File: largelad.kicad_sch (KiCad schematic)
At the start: 297 parts, among them SW1 RotaryEncoder_Switch, U3 YAAJ_WeAct_BlackPill_Part_Like

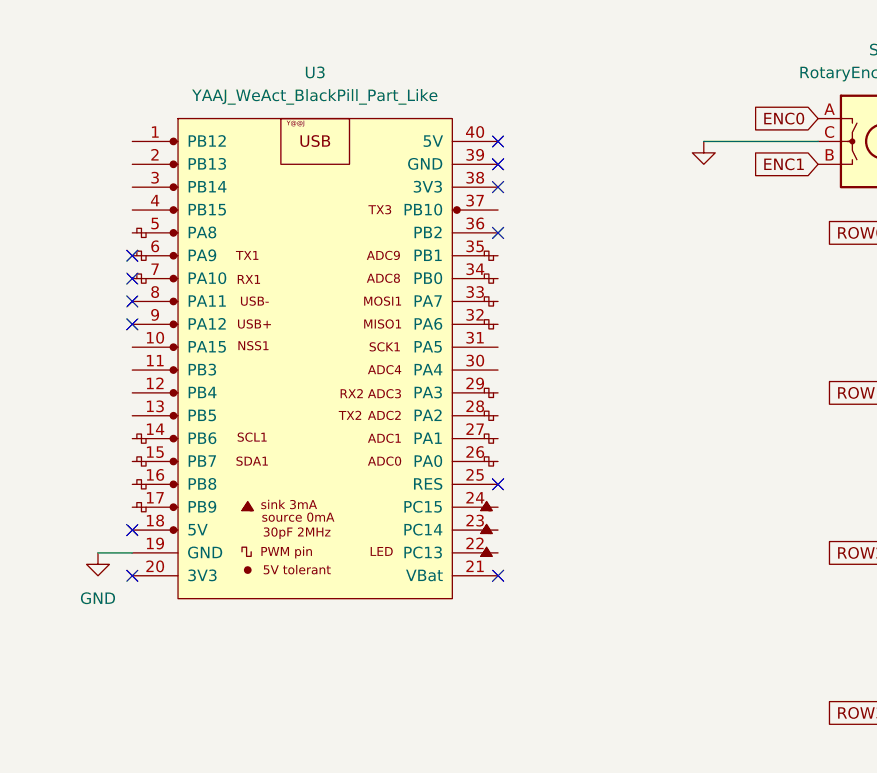
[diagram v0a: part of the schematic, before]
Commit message: connect up the columns
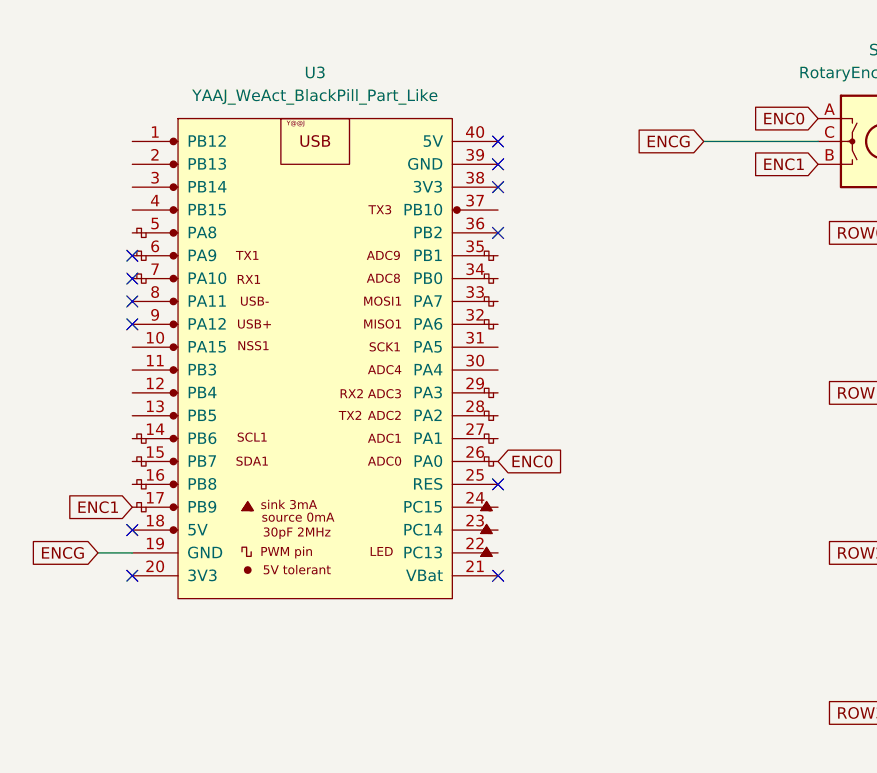
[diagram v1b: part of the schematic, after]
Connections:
- net ENC0: now also U3.26 (PA0)
- net ENC1: now also U3.17 (PB9)
- net GND renamed ENCG
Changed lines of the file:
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@@
     )
   )
+  (global_label "ENC1" (shape input) (at 96.52 74.93 180) (fields_autoplaced)
+    (effects (font (size 1.27 1.27)) (justify right))
+    (property "Intersheet References" "${INTERSHEET_REFS}" (id 0) (at 89.1479 74.8506 0)
+      (effects (font (size 1.27 1.27)) (justify right) hide)
+    )
+  )
   (global_label "COL4" (shape input) (at 240.03 30.48 90) (fields_autoplaced)
     (effects (font (size 1.27 1.27)) (justify left))
@@
     )
   )
+  (global_label "ENCG" (shape input) (at 160.02 34.29 180) (fields_autoplaced)
+    (effects (font (size 1.27 1.27)) (justify right))
+    (property "Intersheet References" "${INTERSHEET_REFS}" (id 0) (at 152.5874 34.2106 0)
+      (effects (font (size 1.27 1.27)) (justify right) hide)
+    )
+  )
   (global_label "ROW1" (shape input) (at 181.61 62.23 180) (fields_autoplaced)
     (effects (font (size 1.27 1.27)) (justify right))
@@
     )
   )
+  (global_label "ENCG" (shape input) (at 92.71 80.01 180) (fields_autoplaced)
+    (effects (font (size 1.27 1.27)) (justify right))
+    (property "Intersheet References" "${INTERSHEET_REFS}" (id 0) (at 85.2774 79.9306 0)
+      (effects (font (size 1.27 1.27)) (justify right) hide)
+    )
+  )
   (global_label "ROW7" (shape input) (at 181.61 168.91 180) (fields_autoplaced)
     (effects (font (size 1.27 1.27)) (justify right))
@@
     )
   )
+  (global_label "ENC0" (shape input) (at 137.16 69.85 0) (fields_autoplaced)
+    (effects (font (size 1.27 1.27)) (justify left))
+    (property "Intersheet References" "${INTERSHEET_REFS}" (id 0) (at 144.5321 69.9294 0)
+      (effects (font (size 1.27 1.27)) (justify left) hide)
+    )
+  )
   (global_label "ROW3" (shape input) (at 181.61 97.79 180) (fields_autoplaced)
     (effects (font (size 1.27 1.27)) (justify right))
@@
     (pin "2")
   )
-  (symbol (lib_id "power:GND") (at 92.71 80.01 0) (unit 1)
-    (in_bom yes) (on_board yes) (fields_autoplaced)
-    (property "Reference" "#PWR03" (id 0) (at 92.71 86.36 0)
-      (effects (font (size 1.27 1.27)) hide)
-    )
-    (property "Value" "GND" (id 1) (at 92.71 85.09 0))
-    (property "Footprint" "" (id 2) (at 92.71 80.01 0)
-      (effects (font (size 1.27 1.27)) hide)
-    )
-    (property "Datasheet" "" (id 3) (at 92.71 80.01 0)
-      (effects (font (size 1.27 1.27)) hide)
-    )
-    (pin "1")
-  )
   (symbol (lib_id "Device:D_Small") (at 187.96 59.69 90) (unit 1)
     (in_bom yes) (on_board yes) (fields_autoplaced)
@@
     (pin "2")
   )
-  (symbol (lib_id "power:GND") (at 160.02 34.29 0) (unit 1)
-    (in_bom yes) (on_board yes) (fields_autoplaced)
-    (property "Reference" "#PWR?" (id 0) (at 160.02 40.64 0)
-      (effects (font (size 1.27 1.27)) hide)
-    )
-    (property "Value" "" (id 1) (at 160.02 39.37 0))
-    (property "Footprint" "" (id 2) (at 160.02 34.29 0)
-      (effects (font (size 1.27 1.27)) hide)
-    )
-    (property "Datasheet" "" (id 3) (at 160.02 34.29 0)
-      (effects (font (size 1.27 1.27)) hide)
-    )
-    (pin "1")
-  )
   (symbol (lib_id "MX_Alps_Hybrid:MX-NoLED") (at 316.23 142.24 0) (unit 1)
     (in_bom yes) (on_board yes) (fields_autoplaced)
@@
   )
   (symbol_instances
-    (path "/04dedb14-e500-439f-b9ef-e11c5c893a28"
-      (reference "#PWR03") (unit 1) (value "GND") (footprint "")
-    )
-    (path "/8a7c29b1-55bb-4abf-a29c-9a4fb18ec56b"
-      (reference "#PWR?") (unit 1) (value "GND") (footprint "")
-    )
     (path "/1bb5c3f3-3c24-465d-aac9-5daa959db6ee"
       (reference "D1") (unit 1) (value "D_Small") (footprint "Diode_THT:D_DO-35_SOD27_P7.62mm_Horizontal")

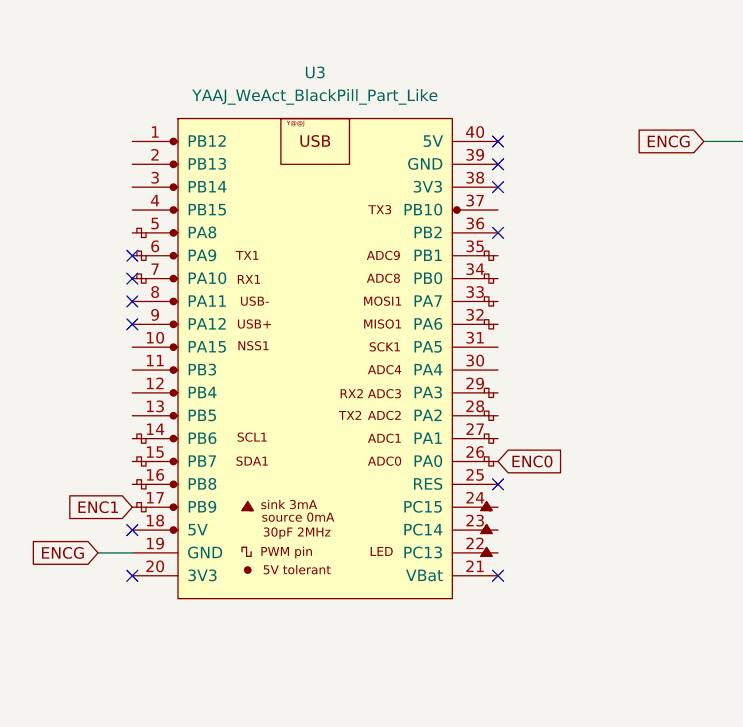
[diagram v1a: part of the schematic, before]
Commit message: route the whole matrix
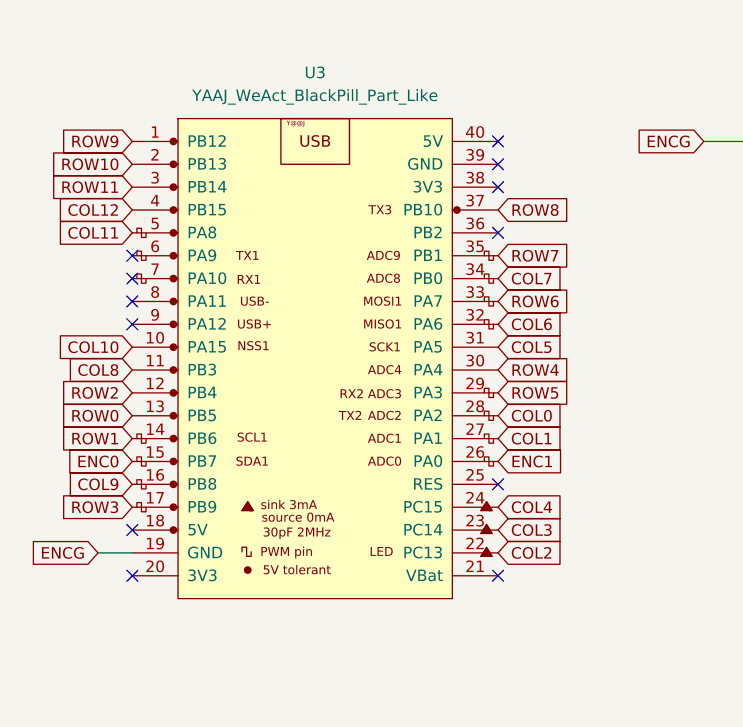
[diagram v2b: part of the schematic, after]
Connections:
- net COL0: now also U3.28 (PA2)
- net COL1: now also U3.27 (PA1)
- net COL10: now also U3.10 (PA15)
- net COL11: now also U3.5 (PA8)
- net COL12: now also U3.4 (PB15)
- net COL2: now also U3.22 (PC13)
- net COL3: now also U3.23 (PC14)
- net COL4: now also U3.24 (PC15)
- net COL5: now also U3.31 (PA5)
- net COL6: now also U3.32 (PA6)
- net COL7: now also U3.34 (PB0)
- net COL8: now also U3.11 (PB3)
- net COL9: now also U3.16 (PB8)
- net ENC0: now also U3.15 (PB7); no longer U3.26 (PA0)
- net ENC1: now also U3.26 (PA0); no longer U3.17 (PB9)
- net ROW0: now also U3.13 (PB5)
- net ROW1: now also U3.14 (PB6)
- net ROW10: now also U3.2 (PB13)
- net ROW11: now also U3.3 (PB14)
- net ROW2: now also U3.12 (PB4)
- net ROW3: now also U3.17 (PB9)
- net ROW4: now also U3.30 (PA4)
- net ROW5: now also U3.29 (PA3)
- net ROW6: now also U3.33 (PA7)
- net ROW7: now also U3.35 (PB1)
- net ROW8: now also U3.37 (PB10)
- net ROW9: now also U3.1 (PB12)
